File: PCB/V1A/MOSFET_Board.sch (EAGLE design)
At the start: 257 parts, among them IC301 7805T, IC302 7805T, J302 FAN_MOLEX4PIN, J303 FAN_MOLEX4PIN, Q201 SIRC10DP, Q202 SIRC10DP, Q203 BC817, Q204 BC817, Q205 SIRC10DP, Q206 SIRC10DP, Q207 BC817, Q208 BC807, Q209 BC817, Q210 BC807, Q211 IXTK102N65X2, Q212 IXTK102N65X2, Q401 BC807, Q402 BC807, Q403 BC807, Q404 BC807, Q405 BC807, Q406 BC807, Q407 BC807, Q408 BC807, Q409 BC807, Q410 BC807, Q411 BC807, Q412 BC807, Q413 BC807, Q414 BC807, U201 AD420, U202 AD420, U203 LT1014I, U204 LT1014I, U205 AD620, U206 AD620, U207 AD620, U208 AD620, U209 LTC1865L, U210 LTC1865L, U301 MAX743, U302 LP2985-3.1, U303 LM50, U304 LM50, U305 AD620, U306 LTC1865L, U307 LTC1865L, U401 HCPL-063N, U402 HCPL-063N, U403 HCPL-063N, U404 HCPL-063N, U405 HCPL-063N, U406 HCPL-063N, U407 HCPL-063N, X301 GMSTBA4

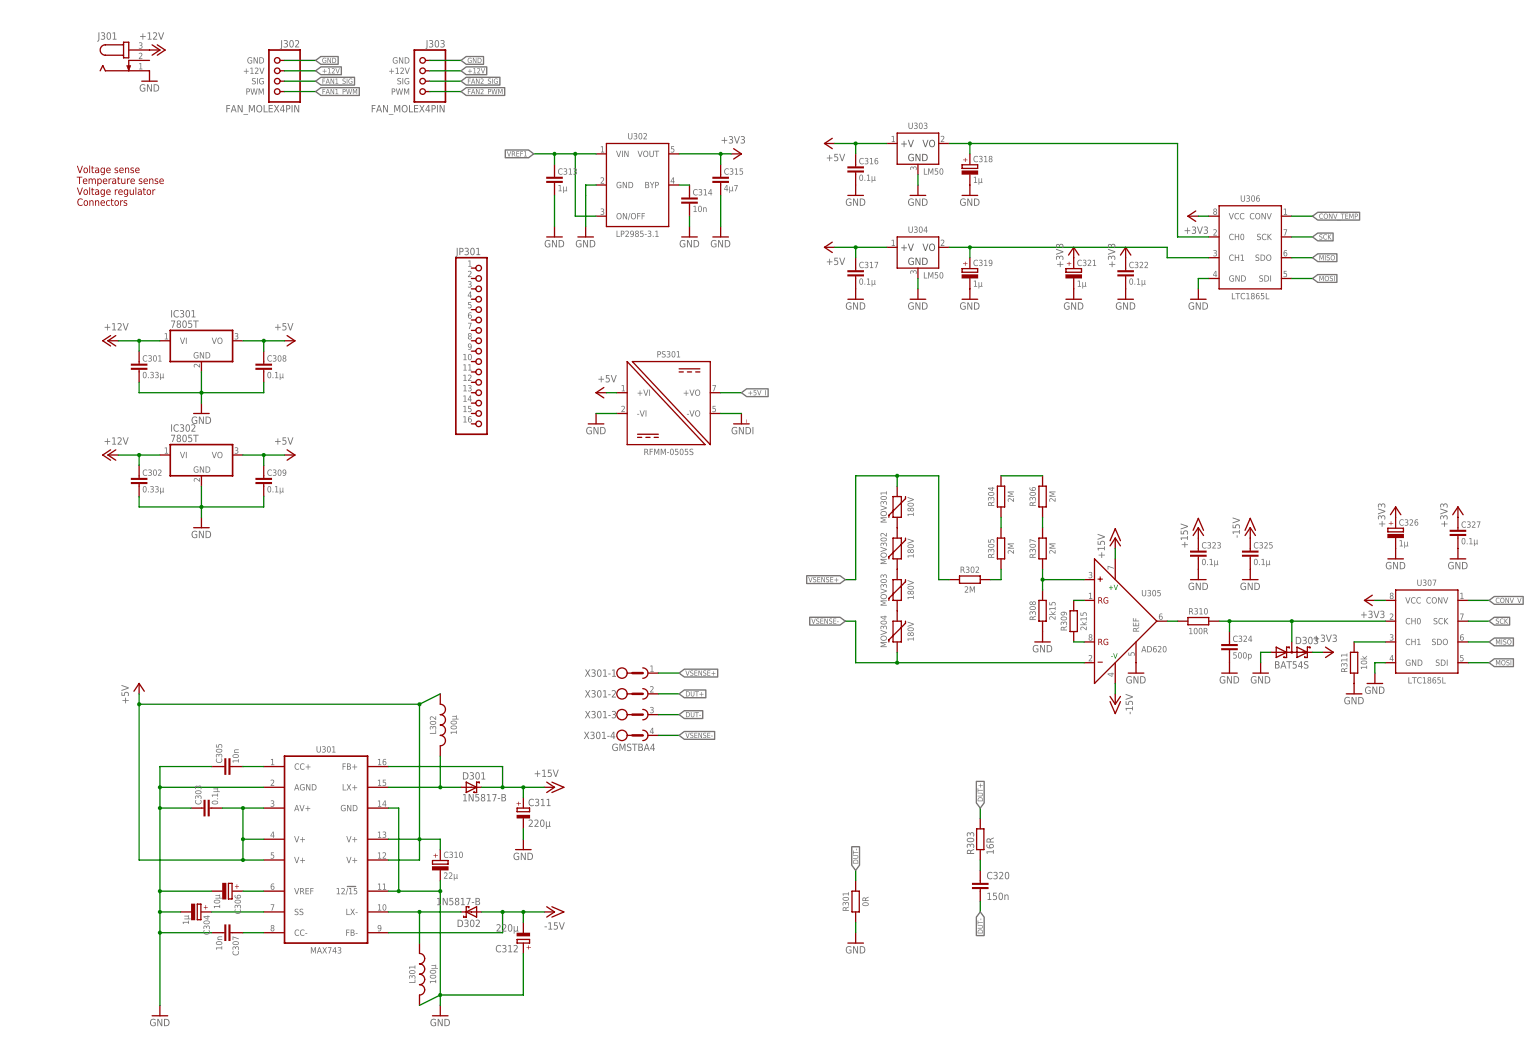
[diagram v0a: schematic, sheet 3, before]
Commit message: Removed abandoned PCB attempts
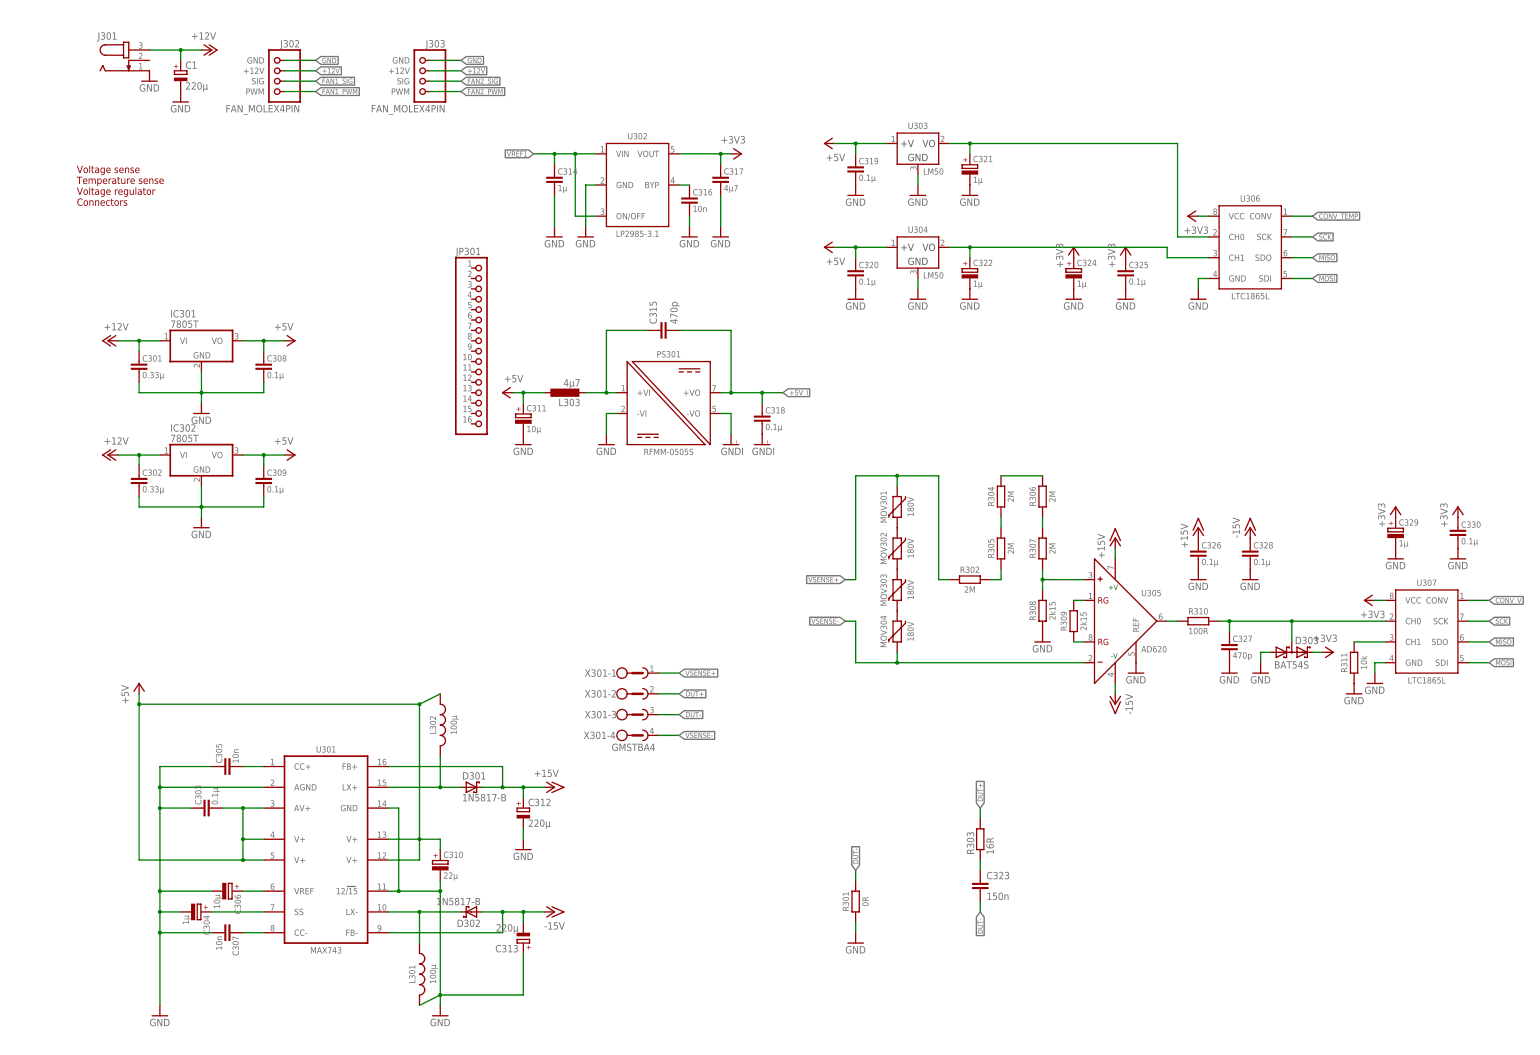
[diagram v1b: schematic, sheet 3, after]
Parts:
- added C1: 220µ, rcl:CPOL-EUE3.5-10
- added C328, C330: 0.1µ, passives:C-EU-1608
- added C329: 1µ, passives:CPOL-3216-A
- added L303: 4µ7, inductor-coilcraft:MSS7341
- C205, C207: value 0.01µ -> 10n
- C206, C208, C405, C406, C407, C408, C420, C421, C422: value 0.01µ -> 10n; device passives:C-EU-3216 -> passives:C-EU-2012
- C225, C226, C227, C228: value 100p -> 470p
- C303, C325: device passives:C-EU-3216 -> passives:C-EU-1608
- C311: value 220µ -> 10µ; device rcl:CPOL-EUE3.5-10 -> passives:CPOL-6032-C
- C313: value 1µ -> 220µ; device passives:C-EU-3216 -> rcl:CPOL-EUE3.5-10
- C314: value 10n -> 1µ; device passives:C-EU-2012 -> passives:C-EU-3216
- C315: value 4µ7 -> 470p; device passives:C-EU-3216 -> rcl:C-EU075-032X103
- C316: value 0.1µ -> 10n; device passives:C-EU-3216 -> passives:C-EU-2012
- C317: value 0.1µ -> 4µ7
- C318, C319, C326: value 1µ -> 0.1µ; device passives:CPOL-3216-A -> passives:C-EU-1608
- C320: value 150n -> 0.1µ; device rcl:C-EU050-030X075 -> passives:C-EU-1608
- C322: value 0.1µ -> 1µ; device passives:C-EU-3216 -> passives:CPOL-3216-A
- C323: value 0.1µ -> 150n; device passives:C-EU-3216 -> rcl:C-EU050-030X075
- C324: value 500p -> 1µ; device passives:C-EU-1608 -> passives:CPOL-3216-A
- C327: value 0.1µ -> 470p; device passives:C-EU-3216 -> passives:C-EU-1608
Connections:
- new net N$60: C315.1, L303.1, PS301.+VI
- net +12V: now also C1.+
- net +15V: now also C312.+, C326.1; no longer C311.+, C323.1
- net +3V3: now also C317.1, C324.+, C325.1, C329.+, C330.1; no longer C315.1, C321.+, C322.1, C326.+, C327.1
- net +5V: now also C311.+, C319.1, C320.1, L303.2; no longer C316.1, C317.1, PS301.+VI
- net +5V_I: now also C315.2, C318.1
- net -15V: now also C313.-, C328.1; no longer C312.-, C325.1
- net DUT-: now also C323.2; no longer C320.2
- net GND: now also C1.-, C312.-, C313.+, C319.2, C320.2, C322.-, C324.-, C326.2, C328.2, C329.-, C330.2; no longer C312.+, C313.2, C315.2, C318.-, C319.-, C322.2, C323.2, C324.2, C326.-
- net GNDI: now also C318.2
- net N$10: now also C316.1; no longer C314.1
- net N$30: now also C327.1; no longer C324.1
- net N$61: now also C323.1; no longer C320.1
- net TEMP1: now also C321.+; no longer C318.+
- net TEMP2: now also C322.+; no longer C319.+
- net VREF1: now also C314.1; no longer C313.1
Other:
- moved on the sheet: C311, C312, C314, C315, C316, C317, C320, C321, C323, C325, C327

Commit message: Finalizing components & placement
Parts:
- removed R301: 0R, passives:R-EU-3216
- removed U303, U304: LM50, ic:LM50
- removed X301: GMSTBA4, con-phoenix-762:GMSTBA4
- added C2: 4µ7, passives:C-EU-3216
- added J1, J2: (no value), mechanical:AMPHENOL_TERM-BLOCK_2
- added JP3: (no value), pinhead:PINHD-2X3
- added SJ1: (no value), jumper:SJW
- C201, C202, C203, C204, C211, C212, C213, C214, C215, C216, C217, C218, C219, C220, C221, C222, C223, C224, C231, C232, C303, C308, C309, C318, C319, C320, C325, C326, C328, C330, C401, C402, C403, C404, C417, C418, C419: value 0.1µ -> 100n
- C209, C210, C229, C230, C324, C329: value 1µ -> 4µ7; device passives:CPOL-3216-A -> passives:C-EU-3216
- C301, C302: value 0.33µ -> 470n; device passives:C-EU-3216 -> passives:C-EU-1608
- C304, C321, C322: value 1µ -> 470n; device passives:CPOL-3216-A -> passives:C-EU-1608
- C310: value 22µ -> 47µ; device passives:CPOL-6032-C -> passives:CPOL-7343-DE
- C314: value 1µ -> 4µ7
- C405, C406, C407, C408, C420, C421, C422: device passives:C-EU-2012 -> passives:C-EU-1608
- R229, R230, R255, R256, R257, R258, R310: device passives:R-EU-2012 -> passives:R-EU-1608
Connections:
- net +3V3: now also C229.1, C230.1, C324.1, C329.1, R410.2, R411.2, R415.2, R419.2; no longer C229.+, C230.+, C324.+, C329.+, R413.2, R426.2, R427.2
- net +5V: now also C2.1, C209.1, C210.1, JP3.3, JP3.4, R413.2, R426.2, R427.2; no longer C209.+, C210.+, R410.2, R411.2, R415.2, R419.2, U303.+V, U304.+V
- net CONV_C1: now also C415.1, R415.1, U403.VO2; no longer C411.1, R411.1, U403.VO1
- net CONV_C1_I: now also Q407.B; no longer Q403.B
- net CONV_C2: now also C416.1, R416.1, U404.VO2; no longer C415.1, R415.1, U403.VO2
- net CONV_C2_I: now also Q408.B; no longer Q407.B
- net CONV_TEMP: now also C411.1, R411.1, U403.VO1; no longer C410.1, R410.1, U402.VO1
- net CONV_TEMP_I: now also Q403.B; no longer Q402.B
- net CONV_V: now also C412.1, R412.1, U404.VO1; no longer C414.1, R414.1, U402.VO2
- net CONV_V_I: now also Q404.B; no longer Q406.B
- net DUT+: now also J1G$2.1; no longer X301-2.1
- net DUT-: now also J2G$1.1, SJ1.2; no longer R301.2, X301-3.1
- net FLT_DAC: now also Q411.B; no longer Q414.B
- net FLT_DAC_I: now also C425.1, R425.1, U407.VO1; no longer C428.1, R428.1, U407.VO2
- net GND: now also C2.2, C209.2, C210.2, C229.2, C230.2, C304.2, C321.2, C322.2, C324.2, C329.2, JP3.1, JP3.2, SJ1.1; no longer C209.-, C210.-, C229.-, C230.-, C304.-, C321.-, C322.-, C324.-, C329.-, R301.1, U303.GND, U304.GND
- net MISO: now also Q414.B; no longer Q411.B
- net MISO_I: now also C428.1, R428.1, U407.VO2; no longer C425.1, R425.1, U407.VO1
- net MOSI: now also C410.1, R410.1, U402.VO1; no longer C416.1, R416.1, U404.VO2
- net MOSI_I: now also Q402.B; no longer Q408.B
- net N$35: now also C304.1; no longer C304.+
- net SCK: now also C414.1, R414.1, U402.VO2; no longer C412.1, R412.1, U404.VO1
- net SCK_I: now also Q406.B; no longer Q404.B
- net TEMP1: now also C321.1, JP3.5; no longer C321.+, U303.VO
- net TEMP2: now also C322.1, JP3.6; no longer C322.+, U304.VO
- net VSENSE+: now also J1G$1.1; no longer X301-1.1
- net VSENSE-: now also J2G$2.1; no longer X301-4.1
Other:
- moved on the sheet: C310, C319, C320, C325

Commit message: Cleaned DOCS
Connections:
- net +5V_I: now also JP301.16
- net BYP_I: now also JP301.8
- net CLR_DAC1_I: now also JP301.6
- net CLR_DAC2_I: now also JP301.5
- net CONV_C1_I: now also JP301.9
- net CONV_C2_I: now also JP301.11
- net CONV_TEMP_I: now also JP301.10
- net CONV_V_I: now also JP301.12
- net FAN1_PWM_I: now also JP301.14
- net FAN2_PWM_I: now also JP301.13
- net FLT_DAC_I: now also JP301.1
- net GNDI: now also JP301.15
- net LATCH_DAC_I: now also JP301.7
- net MISO_I: now also JP301.2
- net MOSI_I: now also JP301.4
- net SCK_I: now also JP301.3
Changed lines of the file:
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@@
 <pinref part="GNDI302" gate="G$1" pin="GNDI"/>
+</segment>
+<segment>
+<pinref part="JP301" gate="A" pin="15"/>
+<wire x1="116.84" y1="160.02" x2="111.76" y2="160.02" width="0.1524" layer="91"/>
+<label x="111.76" y="160.02" size="1.27" layer="95" font="vector" ratio="12" rot="R180" xref="yes"/>
 </segment>
 </net>
@@
 <junction x="187.96" y="165.1"/>
 </segment>
+<segment>
+<pinref part="JP301" gate="A" pin="16"/>
+<wire x1="116.84" y1="157.48" x2="111.76" y2="157.48" width="0.1524" layer="91"/>
+<label x="111.76" y="157.48" size="1.27" layer="95" font="vector" ratio="12" rot="R180" xref="yes"/>
+</segment>
 </net>
 <net name="VREF1" class="0">
@@
 </segment>
 </net>
+<net name="FAN1_PWM_I" class="5">
+<segment>
+<pinref part="JP301" gate="A" pin="14"/>
+<wire x1="116.84" y1="162.56" x2="111.76" y2="162.56" width="0.1524" layer="91"/>
+<label x="111.76" y="162.56" size="1.27" layer="95" font="vector" ratio="12" rot="R180" xref="yes"/>
+</segment>
+</net>
+<net name="FAN2_PWM_I" class="5">
+<segment>
+<pinref part="JP301" gate="A" pin="13"/>
+<wire x1="116.84" y1="165.1" x2="111.76" y2="165.1" width="0.1524" layer="91"/>
+<label x="111.76" y="165.1" size="1.27" layer="95" font="vector" ratio="12" rot="R180" xref="yes"/>
+</segment>
+</net>
+<net name="CONV_V_I" class="5">
+<segment>
+<pinref part="JP301" gate="A" pin="12"/>
+<wire x1="116.84" y1="167.64" x2="111.76" y2="167.64" width="0.1524" layer="91"/>
+<label x="111.76" y="167.64" size="1.27" layer="95" font="vector" ratio="12" rot="R180" xref="yes"/>
+</segment>
+</net>
+<net name="CONV_C2_I" class="5">
+<segment>
+<pinref part="JP301" gate="A" pin="11"/>
+<wire x1="116.84" y1="170.18" x2="111.76" y2="170.18" width="0.1524" layer="91"/>
+<label x="111.76" y="170.18" size="1.27" layer="95" font="vector" ratio="12" rot="R180" xref="yes"/>
+</segment>
+</net>
+<net name="CONV_TEMP_I" class="5">
+<segment>
+<pinref part="JP301" gate="A" pin="10"/>
+<wire x1="116.84" y1="172.72" x2="111.76" y2="172.72" width="0.1524" layer="91"/>
+<label x="111.76" y="172.72" size="1.27" layer="95" font="vector" ratio="12" rot="R180" xref="yes"/>
+</segment>
+</net>
+<net name="CONV_C1_I" class="5">
+<segment>
+<pinref part="JP301" gate="A" pin="9"/>
+<wire x1="116.84" y1="175.26" x2="111.76" y2="175.26" width="0.1524" layer="91"/>
+<label x="111.76" y="175.26" size="1.27" layer="95" font="vector" ratio="12" rot="R180" xref="yes"/>
+</segment>
+</net>
+<net name="BYP_I" class="5">
+<segment>
+<pinref part="JP301" gate="A" pin="8"/>
+<wire x1="116.84" y1="177.8" x2="111.76" y2="177.8" width="0.1524" layer="91"/>
+<label x="111.76" y="177.8" size="1.27" layer="95" font="vector" ratio="12" rot="R180" xref="yes"/>
+</segment>
+</net>
+<net name="LATCH_DAC_I" class="5">
+<segment>
+<pinref part="JP301" gate="A" pin="7"/>
+<wire x1="116.84" y1="180.34" x2="111.76" y2="180.34" width="0.1524" layer="91"/>
+<label x="111.76" y="180.34" size="1.27" layer="95" font="vector" ratio="12" rot="R180" xref="yes"/>
+</segment>
+</net>
+<net name="CLR_DAC1_I" class="5">
+<segment>
+<pinref part="JP301" gate="A" pin="6"/>
+<wire x1="116.84" y1="182.88" x2="111.76" y2="182.88" width="0.1524" layer="91"/>
+<label x="111.76" y="182.88" size="1.27" layer="95" font="vector" ratio="12" rot="R180" xref="yes"/>
+</segment>
+</net>
+<net name="CLR_DAC2_I" class="5">
+<segment>
+<pinref part="JP301" gate="A" pin="5"/>
+<wire x1="116.84" y1="185.42" x2="111.76" y2="185.42" width="0.1524" layer="91"/>
+<label x="111.76" y="185.42" size="1.27" layer="95" font="vector" ratio="12" rot="R180" xref="yes"/>
+</segment>
+</net>
+<net name="MOSI_I" class="5">
+<segment>
+<pinref part="JP301" gate="A" pin="4"/>
+<wire x1="116.84" y1="187.96" x2="111.76" y2="187.96" width="0.1524" layer="91"/>
+<label x="111.76" y="187.96" size="1.27" layer="95" font="vector" ratio="12" rot="R180" xref="yes"/>
+</segment>
+</net>
+<net name="SCK_I" class="5">
+<segment>
+<pinref part="JP301" gate="A" pin="3"/>
+<wire x1="116.84" y1="190.5" x2="111.76" y2="190.5" width="0.1524" layer="91"/>
+<label x="111.76" y="190.5" size="1.27" layer="95" font="vector" ratio="12" rot="R180" xref="yes"/>
+</segment>
+</net>
+<net name="MISO_I" class="5">
+<segment>
+<pinref part="JP301" gate="A" pin="2"/>
+<wire x1="116.84" y1="193.04" x2="111.76" y2="193.04" width="0.1524" layer="91"/>
+<label x="111.76" y="193.04" size="1.27" layer="95" font="vector" ratio="12" rot="R180" xref="yes"/>
+</segment>
+</net>
+<net name="FLT_DAC_I" class="5">
+<segment>
+<pinref part="JP301" gate="A" pin="1"/>
+<wire x1="116.84" y1="195.58" x2="111.76" y2="195.58" width="0.1524" layer="91"/>
+<label x="111.76" y="195.58" size="1.27" layer="95" font="vector" ratio="12" rot="R180" xref="yes"/>
+</segment>
+</net>
